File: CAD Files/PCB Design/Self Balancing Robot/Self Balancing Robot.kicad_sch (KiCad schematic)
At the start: 5 parts, among them M1 Motor_DC, M2 Motor_DC, U1 DEVKIT_V1_ESP32-WROOM-32, U2 TB6612FNG

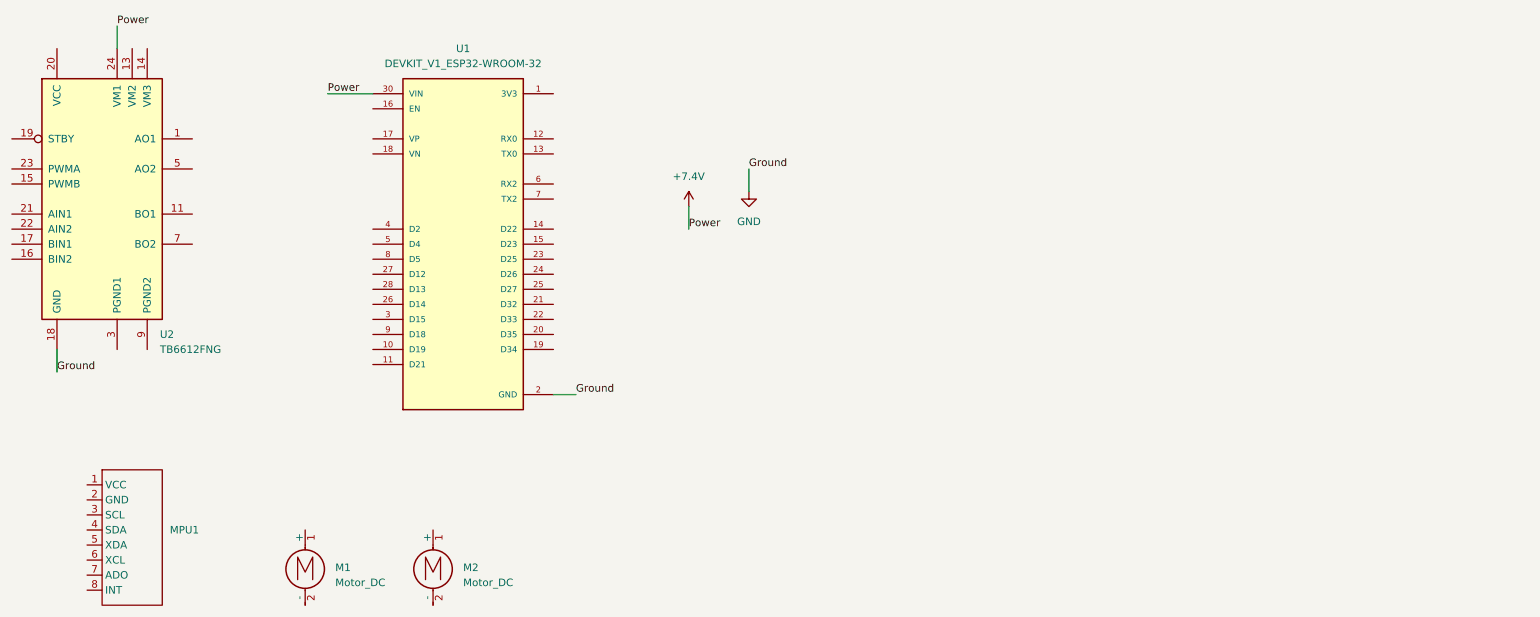
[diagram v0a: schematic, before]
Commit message: Created PCB schematic
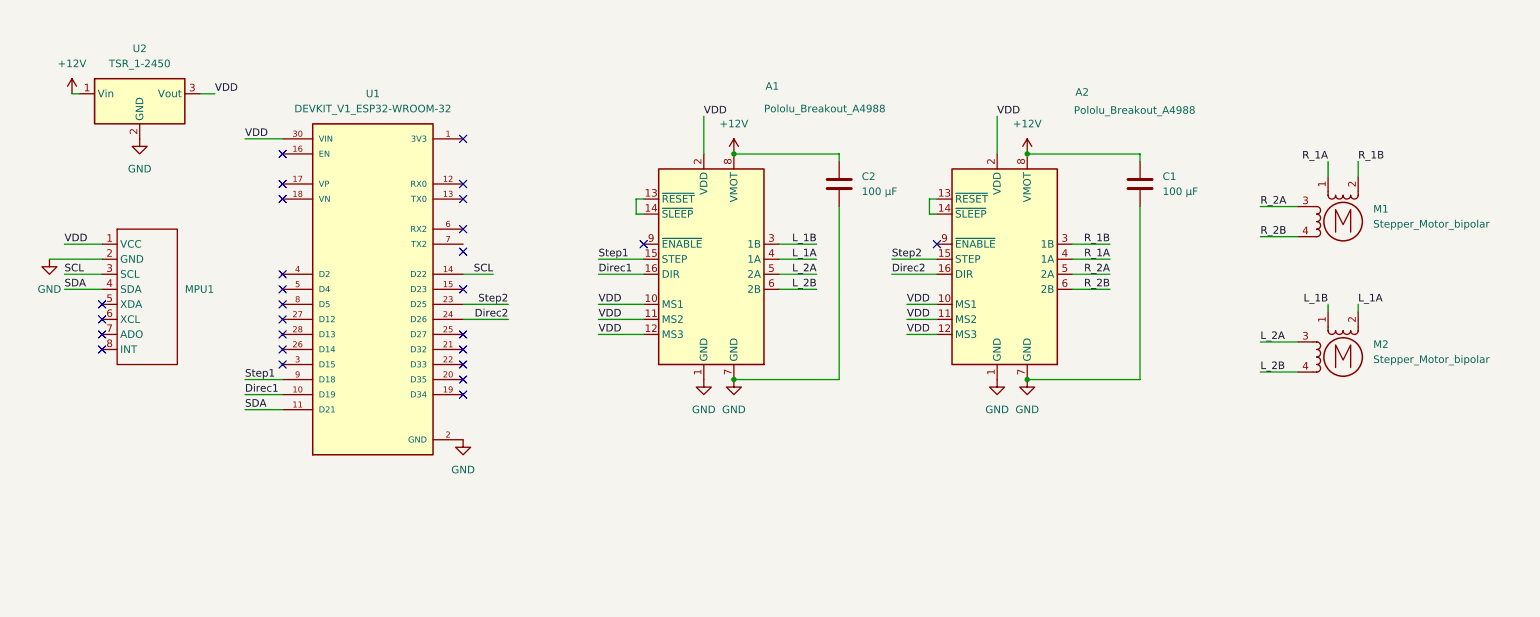
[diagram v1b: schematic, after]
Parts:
- removed M1, M2: Motor_DC, symbol Motor:Motor_DC
- removed U2: TB6612FNG, Package_SO:SSOP-24_5.3x8.2mm_P0.65mm, symbol Driver_Motor:TB6612FNG
- added A1, A2: Pololu_Breakout_A4988, Module:Pololu_Breakout-16_15.2x20.3mm, symbol Driver_Motor:Pololu_Breakout_A4988
- added C1, C2: 100 μF, symbol Device:C
- added M1, M2: Stepper_Motor_bipolar, symbol Motor:Stepper_Motor_bipolar
- added U2: TSR_1-2450, Converter_DCDC:Converter_DCDC_TRACO_TSR-1_THT, symbol Converter_DCDC:TSR_1-2450
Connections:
- net +7.4V is gone; now on net VDD: U1.30 (VIN)
- net GND: now also MPU1.2 (GND), A1.1 (GND), A1.7 (GND), A2.1 (GND), A2.7 (GND), C1.2, C2.2, U2.2 (GND)
- net VDD: now reaches MPU1.1 (VCC)
- net VDD: now also A1.10 (MS1), A1.11 (MS2), A1.12 (MS3), A1.2 (VDD), A2.10 (MS1), A2.11 (MS2), A2.12 (MS3), A2.2 (VDD), U2.3 (Vout)
- net SCL: now reaches MPU1.3 (SCL)
- net SCL: now also U1.14 (D22)
- net SDA: now reaches MPU1.4 (SDA)
- net SDA: now also U1.11 (D21)
- net Direc1: now reaches U1.10 (D19)
- net Direc1: now also A1.16 (DIR)
- net Step2: now reaches U1.23 (D25)
- net Step2: now also A2.15 (STEP)
- net Direc2: now reaches U1.24 (D26)
- net Direc2: now also A2.16 (DIR)
- net Step1: now reaches U1.9 (D18)
- net Step1: now also A1.15 (STEP)
- new net: A2.13 (~{RESET}), A2.14 (~{SLEEP})
- new net: A1.13 (~{RESET}), A1.14 (~{SLEEP})
- new net +12V: A1.8 (VMOT), A2.8 (VMOT), C1.1, C2.1, U2.1 (Vin)
- new net L_1A: A1.4 (1A), M2.2 (-)
- new net L_1B: A1.3 (1B), M2.1
- new net L_2A: A1.5 (2A), M2.3
- new net L_2B: A1.6 (2B), M2.4
- new net R_1A: A2.4 (1A), M1.1
- new net R_1B: A2.3 (1B), M1.2 (-)
- new net R_2A: A2.5 (2A), M1.3
- new net R_2B: A2.6 (2B), M1.4
- no-connect marks 0 -> 27
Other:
- moved on the sheet: MPU1, U1

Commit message: Resolved pin errors
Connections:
- net VDD: now also A1.13 (~{RESET}), A1.14 (~{SLEEP})
